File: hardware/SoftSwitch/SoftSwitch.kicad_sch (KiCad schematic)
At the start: 17 parts, among them J1 80-COLUMN IN, J2 APPLE VIDEO, J3 5-PRONG OUTPUT, J4 4-PRONG OUTPUT, Q1 2N3904, Q2 2N3906, U1 74LS259, U2 74LS259 (passthrough header)

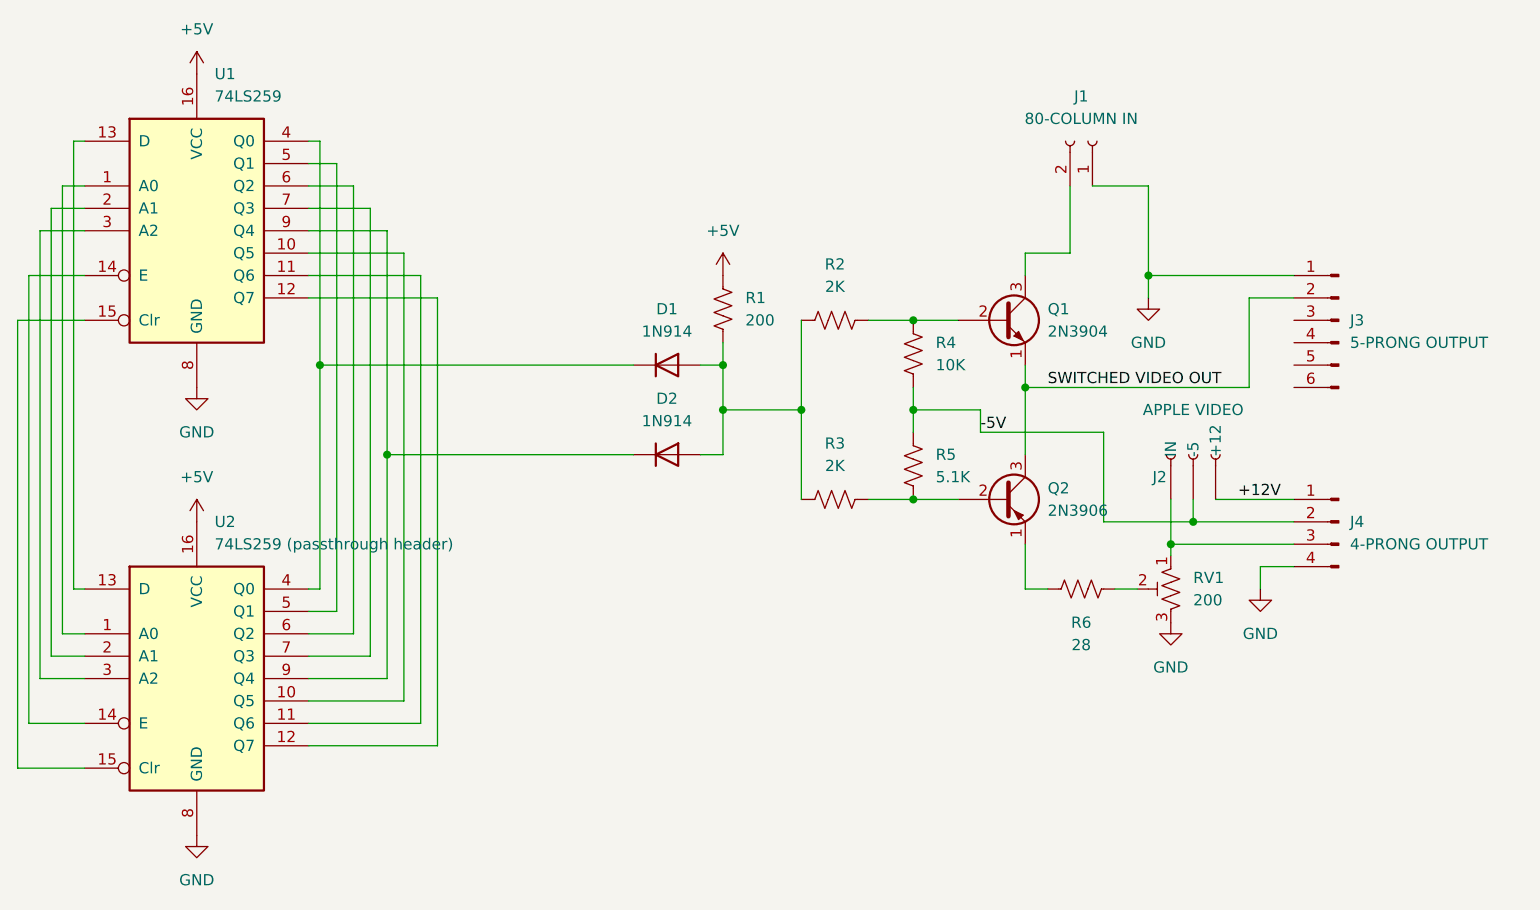
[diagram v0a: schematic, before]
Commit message: make softswitch narrower, general improvements
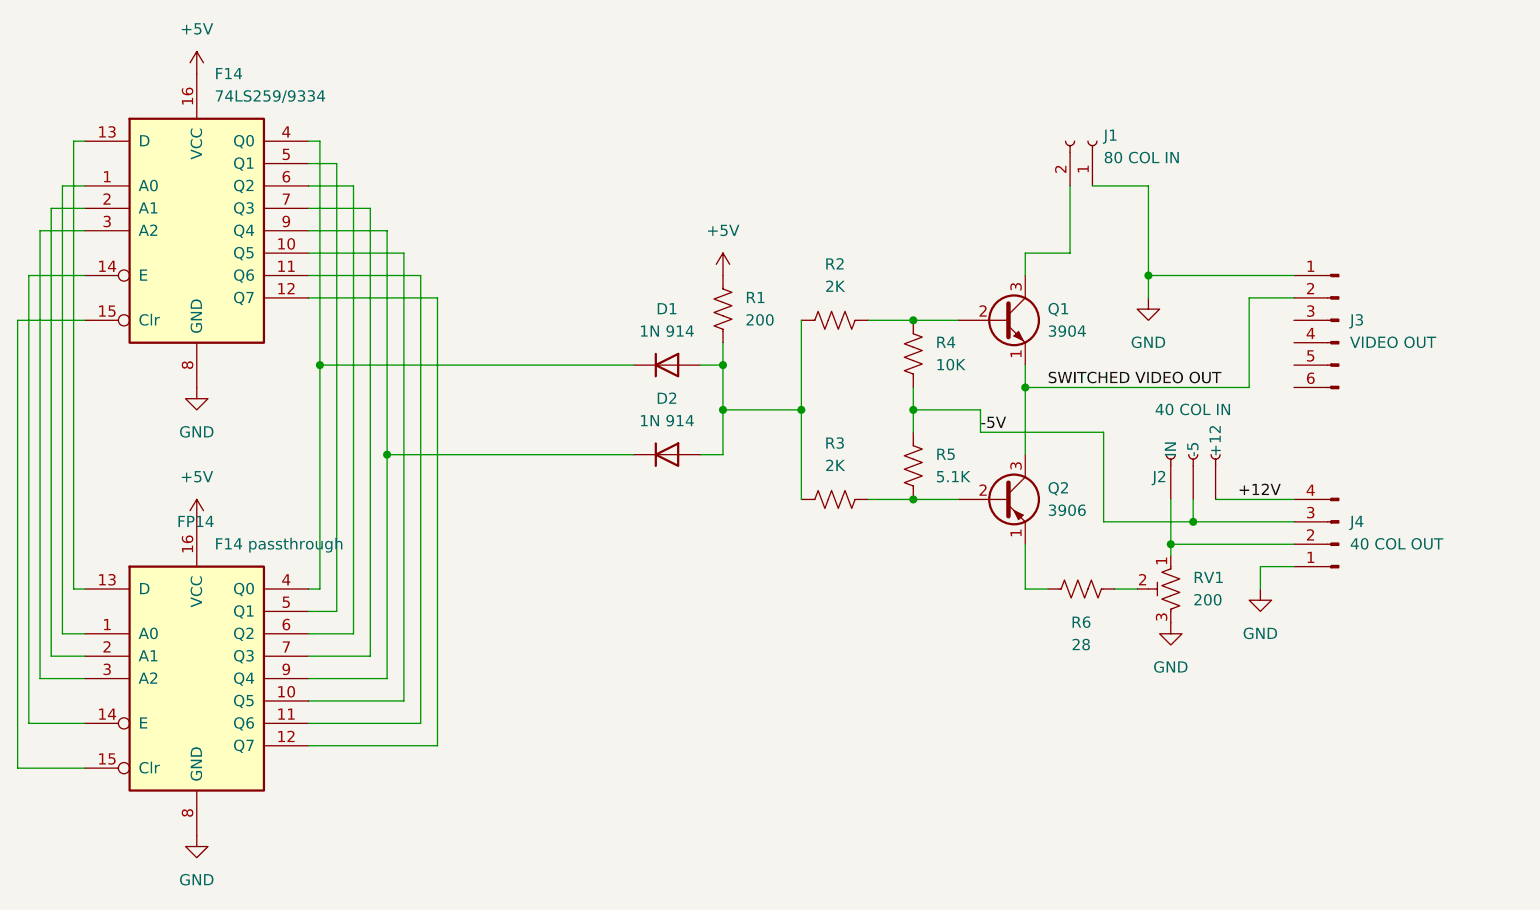
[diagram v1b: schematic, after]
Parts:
- D1, D2: value 1N914 -> 1N 914
- F14: renamed from U1; value 74LS259 -> 74LS259/9334
- FP14: renamed from U2; value 74LS259 (passthrough header) -> F14 passthrough; footprint Package_DIP:DIP-16_W7.62mm -> Package_DIP:DIP-16_W7.62mm_Socket
- J1: value 80-COLUMN IN -> 80 COL IN; footprint Connector_PinHeader_2.54mm:PinHeader_1x02_P2.54mm_Vertical -> Connector_Wire:SolderWire-0.1sqmm_1x02_P3.6mm_D0.4mm_OD1mm_Relief
- J2: value APPLE VIDEO -> 40 COL IN; footprint Connector_PinHeader_2.54mm:PinHeader_1x03_P2.54mm_Vertical -> Connector_Wire:SolderWire-0.1sqmm_1x03_P3.6mm_D0.4mm_OD1mm_Relief
- J3: value 5-PRONG OUTPUT -> VIDEO OUT; footprint Connector_PinHeader_2.54mm:PinHeader_1x06_P2.54mm_Vertical -> Connector_PinHeader_2.54mm:PinHeader_1x06_P2.54mm_Horizontal
- J4: value 4-PRONG OUTPUT -> 40 COL OUT
- Q1: value 2N3904 -> 3904; footprint MyTransistor:TO-92_oldstyle -> Package_TO_SOT_THT:TO-92
- Q2: value 2N3906 -> 3906; footprint MyTransistor:TO-92_oldstyle -> Package_TO_SOT_THT:TO-92
- RV1: footprint Potentiometer_THT:Potentiometer_Bourns_3339H_Vertical -> MyPotentiometer:Multi_Potentiometer_6mm_Vertical
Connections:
- net +12V: now also J4.4 (Pin_4); no longer J4.1 (Pin_1)
- net -5V: now also J4.3 (Pin_3); no longer J4.2 (Pin_2)
- net GND: now also J4.1 (Pin_1); no longer J4.4 (Pin_4)
- net at J2.1 (IN), RV1.1: now also J4.2 (Pin_2); no longer J4.3 (Pin_3)
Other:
- moved on the sheet: J4
